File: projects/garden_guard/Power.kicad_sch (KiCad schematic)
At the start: 50 parts, among them IC1 ACPL-227-50CE, IC2 INA226AQDGSRQ1, IC3 INA226AQDGSRQ1, J7 USB_C_Receptacle_USB2.0, U10 TPS2121RUXR, U11 MAX20408AFOF, U9 Ag5810

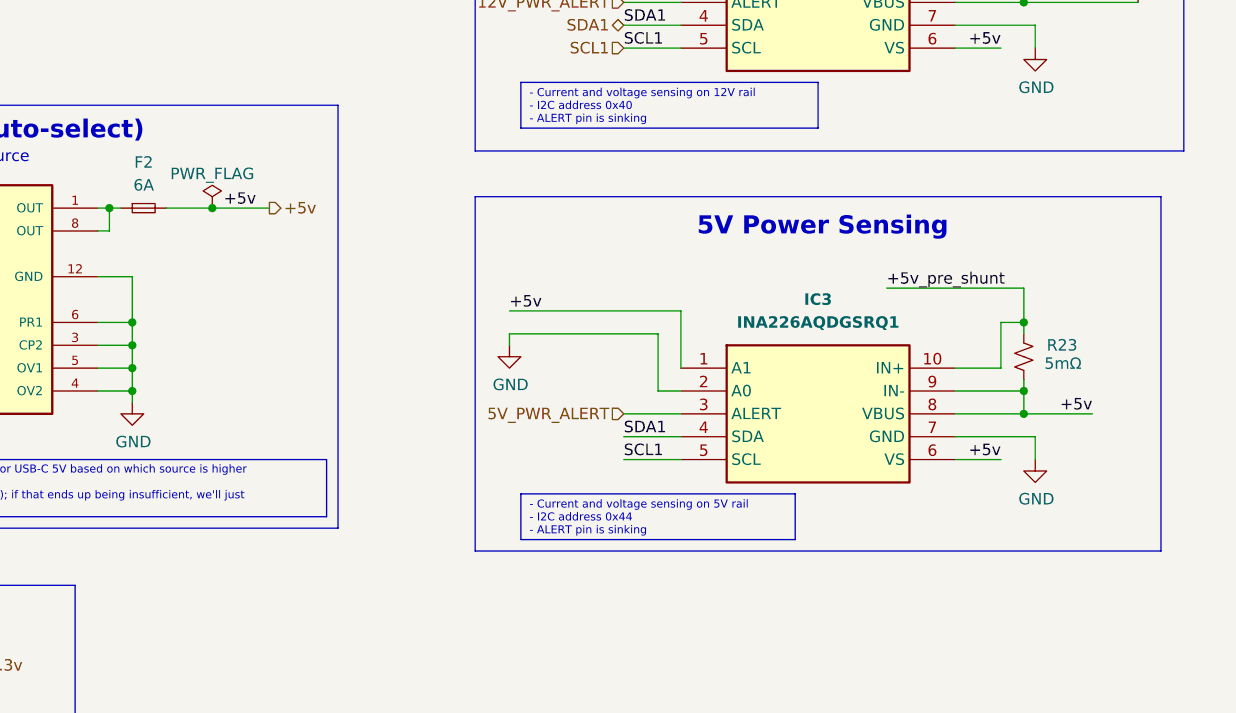
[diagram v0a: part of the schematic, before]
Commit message: 5V and 12V power routing
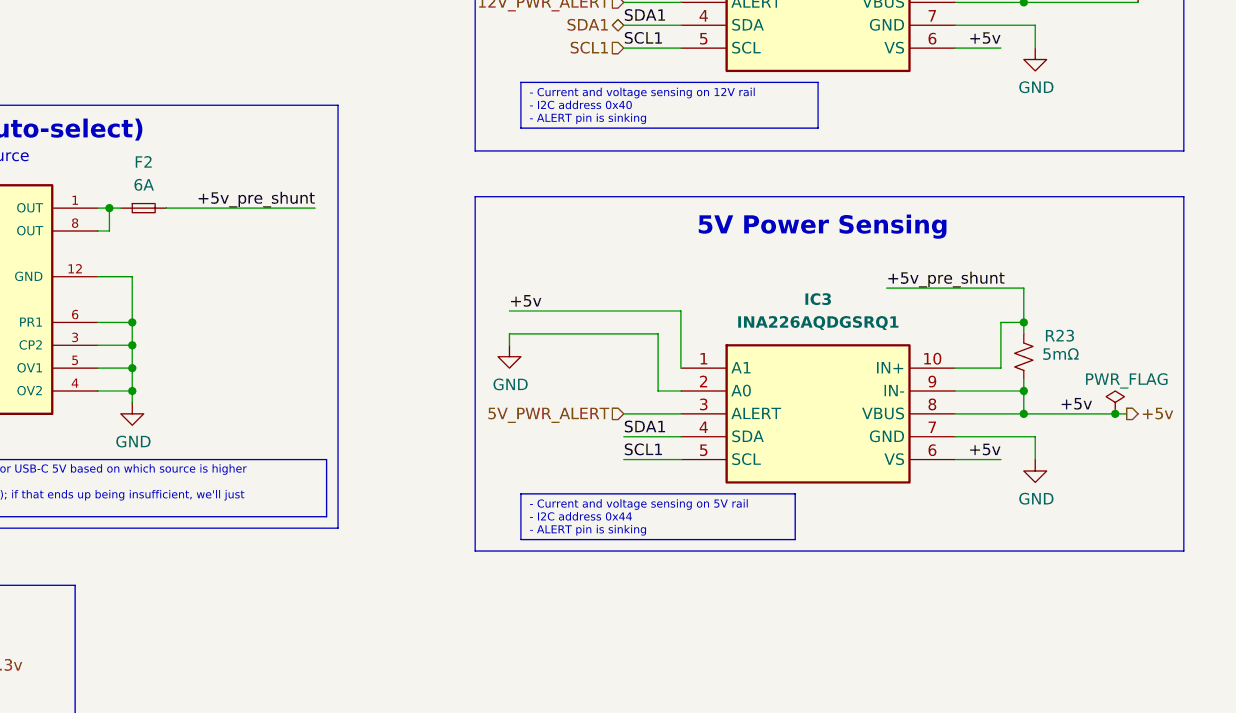
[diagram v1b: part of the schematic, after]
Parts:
- R22, R23: footprint Resistor_SMD:R_0603_1608Metric -> Resistor_SMD:R_2512_6332Metric; LCSC (none) -> C840612; MPN ERJ-3LWFR005V -> CRE2512-FZ-R005E-3; Mfr Panasonic -> Bourns
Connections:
- net +5v: no longer F2.2
- net +5v_pre_shunt: now also F2.2
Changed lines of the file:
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@@
 	(rectangle
 		(start 200.66 123.19)
-		(end 276.86 162.56)
+		(end 279.4 162.56)
 		(stroke
 			(width 0)
@@
 	)
 	(junction
-		(at 171.45 124.46)
-		(diameter 0)
-		(color 0 0 0 0)
-	)
-	(junction
 		(at 93.98 34.29)
 		(diameter 0)
@@
 	)
 	(junction
+		(at 271.78 147.32)
+		(diameter 0)
+		(color 0 0 0 0)
+	)
+	(junction
 		(at 162.56 139.7)
 		(diameter 0)
@@
 	(wire
 		(pts
-			(xy 171.45 124.46) (xy 177.8 124.46)
+			(xy 166.37 124.46) (xy 182.88 124.46)
 		)
 		(stroke
@@
 	(wire
 		(pts
-			(xy 166.37 124.46) (xy 171.45 124.46)
-		)
-		(stroke
-			(width 0)
-			(type default)
-		)
-	)
-	(wire
-		(pts
 			(xy 210.82 26.67) (xy 209.55 26.67)
 		)
@@
 	(wire
 		(pts
+			(xy 271.78 147.32) (xy 273.05 147.32)
+		)
+		(stroke
+			(width 0)
+			(type default)
+		)
+	)
+	(wire
+		(pts
 			(xy 86.36 59.69) (xy 90.17 59.69)
 		)
@@
 	(wire
 		(pts
-			(xy 261.62 147.32) (xy 269.24 147.32)
+			(xy 261.62 147.32) (xy 271.78 147.32)
 		)
 		(stroke
@@
 		)
 	)
-	(label "+5v"
-		(at 172.72 124.46 0)
+	(label "+3.3v"
+		(at 107.95 130.81 0)
 		(effects
 			(font
@@
 		)
 	)
-	(label "+3.3v"
-		(at 107.95 130.81 0)
+	(label "+5v_pre_shunt"
+		(at 182.88 124.46 180)
 		(effects
 			(font
 				(size 1.27 1.27)
 			)
-			(justify left bottom)
+			(justify right bottom)
 		)
 	)
@@
 		)
 	)
+	(hierarchical_label "+5v"
+		(shape output)
+		(at 273.05 147.32 0)
+		(effects
+			(font
+				(size 1.27 1.27)
+			)
+			(justify left)
+		)
+	)
 	(hierarchical_label "SCL1"
 		(shape input)
@@
 		)
 	)
-	(hierarchical_label "+5v"
-		(shape output)
-		(at 177.8 124.46 0)
-		(effects
-			(font
-				(size 1.27 1.27)
-			)
-			(justify left)
-		)
-	)
 	(hierarchical_label "PoE+_actv"
 		(shape output)
@@
 	)
 	(symbol
+		(lib_id "Device:R_Small_US")
+		(at 261.62 140.97 0)
+		(unit 1)
+		(exclude_from_sim no)
+		(in_bom yes)
+		(on_board yes)
+		(dnp no)
+		(property "Reference" "R23"
+			(at 263.906 138.684 0)
+			(effects
+				(font
+					(size 1.27 1.27)
+				)
+				(justify left)
+			)
+		)
+		(property "Value" "5mΩ"
+			(at 263.652 140.7161 0)
+			(effects
+				(font
+					(size 1.27 1.27)
+				)
+				(justify left)
+			)
+		)
+		(property "Footprint" "Resistor_SMD:R_2512_6332Metric"
+			(at 261.62 140.97 0)
+			(effects
+				(font
+					(size 1.27 1.27)
+				)
+				(hide yes)
+			)
+		)
+		(property "Datasheet" "~"
+			(at 261.62 140.97 0)
+			(effects
+				(font
+					(size 1.27 1.27)
+				)
+				(hide yes)
+			)
+		)
+		(property "Description" "Resistor, small US symbol"
+			(at 261.62 140.97 0)
+			(effects
+				(font
+					(size 1.27 1.27)
+				)
+				(hide yes)
+			)
+		)
+		(property "MPN" "CRE2512-FZ-R005E-3"
+			(at 261.62 140.97 0)
+			(effects
+				(font
+					(size 1.27 1.27)
+				)
+				(hide yes)
+			)
+		)
+		(property "Mfr" "Bourns"
+			(at 261.62 140.97 0)
+			(effects
+				(font
+					(size 1.27 1.27)
+				)
+				(hide yes)
+			)
+		)
+		(property "LCSC" "C840612"
+			(at 261.62 140.97 0)
+			(effects
+				(font
+					(size 1.27 1.27)
+				)
+				(hide yes)
+			)
+		)
+		(pin "1"
+		)
+		(pin "2"
+		)
+		(instances
+			(project "garden_guard"
+				(path "/dcdac9d4-ef08-426f-b97c-7b9219501e71/446b5b12-2582-472d-9a1e-c1c7d43f42d1"
+					(reference "R23")
+					(unit 1)
+				)
+			)
+		)
+	)
+	(symbol
 		(lib_id "Device:Fuse_Small")
 		(at 153.67 31.75 0)
@@
 			)
 		)
-		(property "Footprint" "Resistor_SMD:R_0603_1608Metric"
+		(property "Footprint" "Resistor_SMD:R_2512_6332Metric"
 			(at 261.62 95.25 0)
 			(effects
@@
 			)
 		)
-		(property "MPN" "ERJ-3LWFR005V"
+		(property "MPN" "CRE2512-FZ-R005E-3"
 			(at 261.62 95.25 0)
 			(effects
@@
 			)
 		)
-		(property "Mfr" "Panasonic"
+		(property "Mfr" "Bourns"
+			(at 261.62 95.25 0)
+			(effects
+				(font
+					(size 1.27 1.27)
+				)
+				(hide yes)
+			)
+		)
+		(property "LCSC" "C840612"
 			(at 261.62 95.25 0)
 			(effects
@@
 	)
 	(symbol
-		(lib_id "Device:R_Small_US")
-		(at 261.62 140.97 0)
-		(unit 1)
-		(exclude_from_sim no)
-		(in_bom yes)
-		(on_board yes)
-		(dnp no)
-		(property "Reference" "R23"
-			(at 264.16 139.6999 0)
-			(effects
-				(font
-					(size 1.27 1.27)
-				)
-				(justify left)
-			)
-		)
-		(property "Value" "5mΩ"
-			(at 263.906 141.732 0)
-			(effects
-				(font
-					(size 1.27 1.27)
-				)
-				(justify left)
-			)
-		)
-		(property "Footprint" "Resistor_SMD:R_0603_1608Metric"
-			(at 261.62 140.97 0)
-			(effects
-				(font
-					(size 1.27 1.27)
-				)
-				(hide yes)
-			)
-		)
-		(property "Datasheet" "~"
-			(at 261.62 140.97 0)
-			(effects
-				(font
-					(size 1.27 1.27)
-				)
-				(hide yes)
-			)
-		)
-		(property "Description" "Resistor, small US symbol"
-			(at 261.62 140.97 0)
-			(effects
-				(font
-					(size 1.27 1.27)
-				)
-				(hide yes)
-			)
-		)
-		(property "MPN" "ERJ-3LWFR005V"
-			(at 261.62 140.97 0)
-			(effects
-				(font
-					(size 1.27 1.27)
-				)
-				(hide yes)
-			)
-		)
-		(property "Mfr" "Panasonic"
-			(at 261.62 140.97 0)
-			(effects
-				(font
-					(size 1.27 1.27)
-				)
-				(hide yes)
-			)
-		)
-		(pin "1"
-		)
-		(pin "2"
-		)
-		(instances
-			(project "garden_guard"
-				(path "/dcdac9d4-ef08-426f-b97c-7b9219501e71/446b5b12-2582-472d-9a1e-c1c7d43f42d1"
-					(reference "R23")
-					(unit 1)
-				)
-			)
-		)
-	)
-	(symbol
 		(lib_id "Device:C_Small")
 		(at 273.05 50.8 0)
@@
 	(symbol
 		(lib_id "power:PWR_FLAG")
-		(at 171.45 124.46 0)
+		(at 271.78 147.32 0)
 		(unit 1)
 		(exclude_from_sim no)
@@
 		(dnp no)
 		(property "Reference" "#FLG05"
-			(at 171.45 122.555 0)
+			(at 271.78 145.415 0)
 			(effects
 				(font
@@
 		)
 		(property "Value" "PWR_FLAG"
-			(at 171.45 120.65 0)
+			(at 273.05 143.51 0)
 			(effects
 				(font
@@
 		)
 		(property "Footprint" ""
-			(at 171.45 124.46 0)
+			(at 271.78 147.32 0)
 			(effects
 				(font
@@
 		)
 		(property "Datasheet" "~"
-			(at 171.45 124.46 0)
+			(at 271.78 147.32 0)
 			(effects
 				(font
@@
 		)
 		(property "Description" "Special symbol for telling ERC where power comes from"
-			(at 171.45 124.46 0)
+			(at 271.78 147.32 0)
 			(effects
 				(font
